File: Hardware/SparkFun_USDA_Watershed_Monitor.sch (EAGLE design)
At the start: 125 parts, among them J10 QWIIC_RIGHT_ANGLE, J12 3-PIN SMD, J3 QWIIC_RIGHT_ANGLE, J4 U.FL, J5 RJ45, J7 RJ45, J9 RJ45, Q1 20V/4.2A/52mΩ/1.4W, Q10 20V/4.2A/52mΩ/1.4W, Q11 20V/0.2A/8MHz/1.2Ω/1Vth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

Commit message: Update GPIO net names
Include both the ESP GPIO number, and the destination
Required schematic to be nudged around in a couple places
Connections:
- net !RFM_CS! renamed ESP_IO15/!RFM_CS!
- net !RFM_RST! renamed ESP_IO5/!RFM_RST!
- net ESP_I36 renamed ESP_I36/GPS_TX
- net ESP_INT_COM renamed ESP_IO4/INT_COM
- net ESP_IO0_BOOT renamed ESP_IO0/BOOT
- net ESP_IO16 renamed ESP_IO16/VOUT
- net ESP_RX renamed ESP_IO3/ESP_RX
- net ESP_TX renamed ESP_IO1/ESP_TX
- net PICO renamed ESP_IO13/PICO
- net POCI renamed ESP_IO12/POCI
- net RFM_IO0 renamed ESP_IO27/RFM_IO0
- net RFM_IO1 renamed ESP_IO26/RFM_IO1
- net SCK renamed ESP_IO14/SCK
- net SCL renamed ESP_IO22/SCL
- net SDA renamed ESP_IO21/SDA
- net STAT renamed ESP_IO2/STAT
- net V_BATT_2 renamed ESP_IO32/V_BATT_2
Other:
- moved on the sheet: BOOT, C14, C19, C20, C21, C22, C23, C4, C5, C6, CHG, D2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

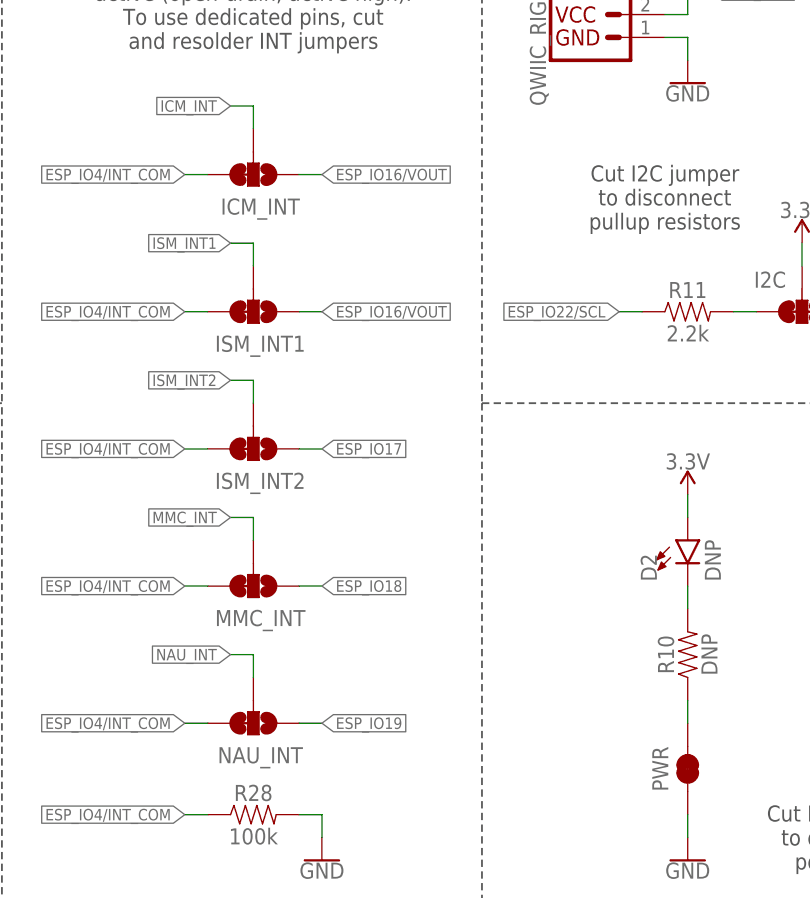
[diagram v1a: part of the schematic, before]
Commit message: Reorder alternative interrupt pins
ESP16 was shared between an alternative interrupt, and the power control
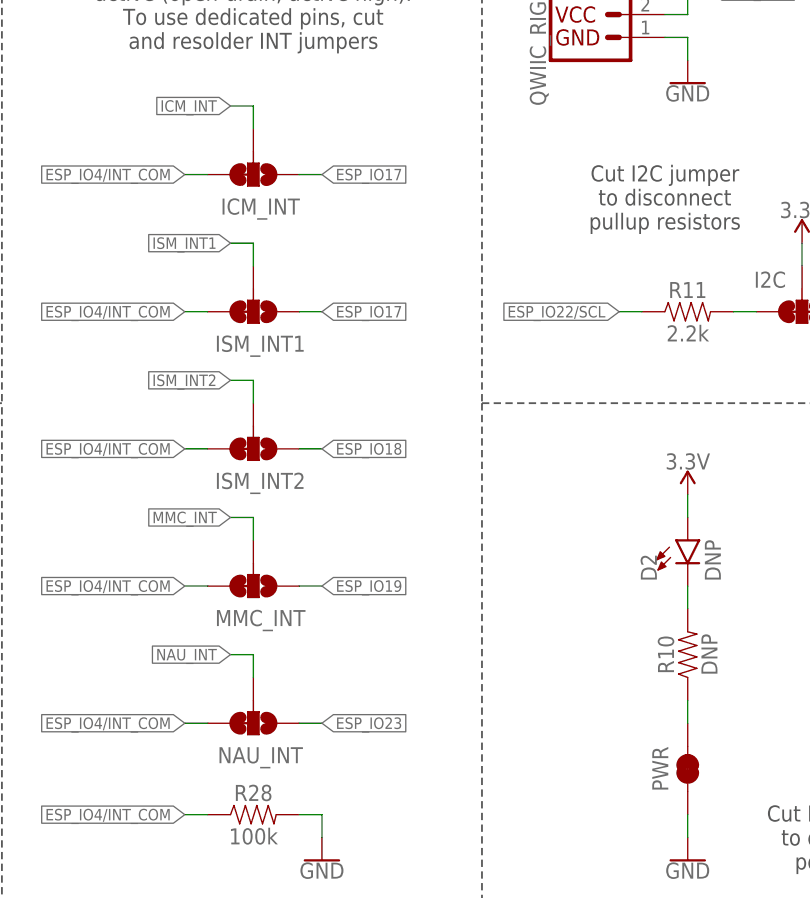
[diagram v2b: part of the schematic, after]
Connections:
- net ESP_IO16/VOUT: no longer ICM_INT.1, ISM_INT1.1
- net ESP_IO17: now also ICM_INT.1, ISM_INT1.1; no longer ISM_INT2.1
- net ESP_IO18: now also ISM_INT2.1; no longer MMC_INT.1
- net ESP_IO19: now also MMC_INT.1; no longer NAU_INT.1
- net ESP_IO23: now also NAU_INT.1
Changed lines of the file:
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@@
-</segment>
-<segment>
-<pinref part="ISM_INT1" gate="G$1" pin="1"/>
-<wire x1="337.82" y1="160.02" x2="340.36" y2="160.02" width="0.1524" layer="91"/>
-<label x="340.36" y="160.02" size="1.27" layer="95" font="vector" xref="yes"/>
-</segment>
-<segment>
-<pinref part="ICM_INT" gate="G$1" pin="1"/>
-<wire x1="337.82" y1="175.26" x2="340.36" y2="175.26" width="0.1524" layer="91"/>
-<label x="340.36" y="175.26" size="1.27" layer="95" font="vector" xref="yes"/>
 </segment>
 <segment>
@@
 </segment>
 <segment>
-<pinref part="ISM_INT2" gate="G$1" pin="1"/>
-<wire x1="337.82" y1="144.78" x2="340.36" y2="144.78" width="0.1524" layer="91"/>
-<label x="340.36" y="144.78" size="1.27" layer="95" font="vector" xref="yes"/>
-</segment>
-<segment>
 <wire x1="307.34" y1="30.48" x2="294.64" y2="30.48" width="0.1524" layer="91"/>
 <label x="294.64" y="30.48" size="1.27" layer="95" font="vector" rot="R180" xref="yes"/>
 <pinref part="J9" gate="JP1" pin="1"/>
+</segment>
+<segment>
+<wire x1="337.82" y1="160.02" x2="340.36" y2="160.02" width="0.1524" layer="91"/>
+<label x="340.36" y="160.02" size="1.27" layer="95" font="vector" xref="yes"/>
+<pinref part="ISM_INT1" gate="G$1" pin="1"/>
+</segment>
+<segment>
+<wire x1="337.82" y1="175.26" x2="340.36" y2="175.26" width="0.1524" layer="91"/>
+<label x="340.36" y="175.26" size="1.27" layer="95" font="vector" xref="yes"/>
+<pinref part="ICM_INT" gate="G$1" pin="1"/>
 </segment>
 </net>
@@
 </segment>
 <segment>
-<pinref part="MMC_INT" gate="G$1" pin="1"/>
-<wire x1="337.82" y1="129.54" x2="340.36" y2="129.54" width="0.1524" layer="91"/>
-<label x="340.36" y="129.54" size="1.27" layer="95" font="vector" xref="yes"/>
-</segment>
-<segment>
 <wire x1="307.34" y1="27.94" x2="294.64" y2="27.94" width="0.1524" layer="91"/>
 <label x="294.64" y="27.94" size="1.27" layer="95" font="vector" rot="R180" xref="yes"/>
 <pinref part="J9" gate="JP1" pin="2"/>
+</segment>
+<segment>
+<wire x1="337.82" y1="144.78" x2="340.36" y2="144.78" width="0.1524" layer="91"/>
+<label x="340.36" y="144.78" size="1.27" layer="95" font="vector" xref="yes"/>
+<pinref part="ISM_INT2" gate="G$1" pin="1"/>
 </segment>
 </net>
@@
 </segment>
 <segment>
-<pinref part="NAU_INT" gate="G$1" pin="1"/>
-<wire x1="337.82" y1="114.3" x2="340.36" y2="114.3" width="0.1524" layer="91"/>
-<label x="340.36" y="114.3" size="1.27" layer="95" font="vector" xref="yes"/>
-</segment>
-<segment>
 <wire x1="307.34" y1="25.4" x2="294.64" y2="25.4" width="0.1524" layer="91"/>
 <label x="294.64" y="25.4" size="1.27" layer="95" font="vector" rot="R180" xref="yes"/>
 <pinref part="J9" gate="JP1" pin="3"/>
+</segment>
+<segment>
+<wire x1="337.82" y1="129.54" x2="340.36" y2="129.54" width="0.1524" layer="91"/>
+<label x="340.36" y="129.54" size="1.27" layer="95" font="vector" xref="yes"/>
+<pinref part="MMC_INT" gate="G$1" pin="1"/>
 </segment>
 </net>
@@
 <pinref part="J9" gate="JP1" pin="4"/>
 </segment>
+<segment>
+<pinref part="NAU_INT" gate="G$1" pin="1"/>
+<wire x1="337.82" y1="114.3" x2="340.36" y2="114.3" width="0.1524" layer="91"/>
+<label x="340.36" y="114.3" size="1.27" layer="95" font="vector" xref="yes"/>
+</segment>
 </net>

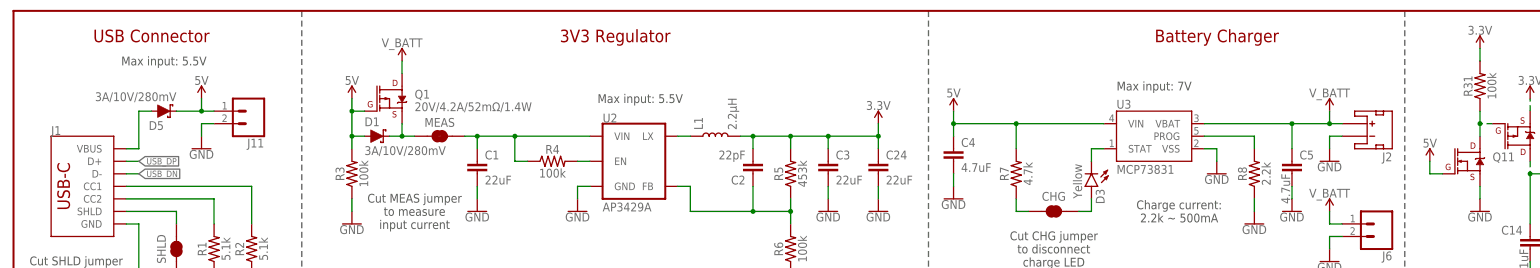
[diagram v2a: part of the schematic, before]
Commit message: Change CH340 power control to be based on VUSB instead of 5V net
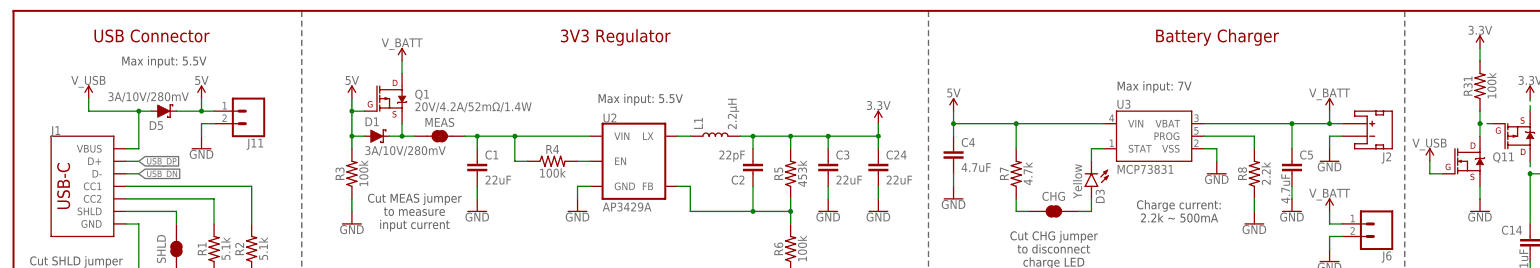
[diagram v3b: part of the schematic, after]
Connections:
- net 5V: no longer Q11.G
- net V_USB: now also Q11.G
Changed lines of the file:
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@@
 <part name="R31" library="SparkFun-Resistors" deviceset="100KOHM" device="-0603-1/10W-1%" value="100k"/>
 <part name="GND63" library="SparkFun-PowerSymbols" deviceset="GND" device=""/>
-<part name="SUPPLY56" library="SparkFun-PowerSymbols" deviceset="5V" device=""/>
 <part name="SUPPLY31" library="SparkFun-PowerSymbols" deviceset="3.3V" device=""/>
 <part name="SUPPLY57" library="SparkFun-PowerSymbols" deviceset="3.3V" device=""/>
 <part name="SUPPLY58" library="SparkFun-PowerSymbols" deviceset="VOUT" device=""/>
+<part name="SUPPLY59" library="SparkFun-PowerSymbols" deviceset="V_USB" device=""/>
+<part name="SUPPLY60" library="SparkFun-PowerSymbols" deviceset="V_USB" device=""/>
 </parts>
 <sheets>
@@
 <instance part="D5" gate="G$1" x="30.48" y="259.08" smashed="yes">
 <attribute name="NAME" x="30.48" y="257.048" size="1.778" layer="95" font="vector" rot="R180"/>
-<attribute name="VALUE" x="33.02" y="261.112" size="1.778" layer="96" font="vector" rot="R180" align="top-left"/>
+<attribute name="VALUE" x="35.56" y="261.112" size="1.778" layer="96" font="vector" rot="R180" align="top-left"/>
 </instance>
 <instance part="SUPPLY2" gate="G$1" x="38.1" y="261.62" smashed="yes">
@@
 <attribute name="VALUE" x="297.18" y="238.506" size="1.778" layer="96" font="vector" align="top-center"/>
 </instance>
-<instance part="SUPPLY56" gate="G$1" x="287.02" y="248.92" smashed="yes">
-<attribute name="VALUE" x="287.02" y="251.714" size="1.778" layer="96" font="vector" align="bottom-center"/>
-</instance>
 <instance part="SUPPLY31" gate="G$1" x="307.34" y="261.62" smashed="yes">
 <attribute name="VALUE" x="307.34" y="264.414" size="1.778" layer="96" font="vector" align="bottom-center"/>
@@
 <instance part="SUPPLY58" gate="G$1" x="297.18" y="33.02" smashed="yes">
 <attribute name="VALUE" x="297.18" y="35.814" size="1.778" layer="96" font="vector" align="bottom-center"/>
+</instance>
+<instance part="SUPPLY59" gate="G$1" x="15.24" y="261.62" smashed="yes">
+<attribute name="VALUE" x="15.24" y="264.414" size="1.778" layer="96" font="vector" align="bottom-center"/>
+</instance>
+<instance part="SUPPLY60" gate="G$1" x="287.02" y="248.92" smashed="yes">
+<attribute name="VALUE" x="287.02" y="251.714" size="1.778" layer="96" font="vector" align="bottom-center"/>
 </instance>
 </instances>
@@
 <wire x1="25.4" y1="259.08" x2="25.4" y2="251.46" width="0.1524" layer="91"/>
 <wire x1="25.4" y1="251.46" x2="22.86" y2="251.46" width="0.1524" layer="91"/>
+<pinref part="SUPPLY59" gate="G$1" pin="V_USB"/>
+<junction x="25.4" y="259.08"/>
+<wire x1="15.24" y1="261.62" x2="15.24" y2="259.08" width="0.1524" layer="91"/>
+<wire x1="15.24" y1="259.08" x2="25.4" y2="259.08" width="0.1524" layer="91"/>
+</segment>
+<segment>
+<pinref part="Q11" gate="NMOS" pin="G"/>
+<wire x1="289.56" y1="246.38" x2="287.02" y2="246.38" width="0.1524" layer="91"/>
+<wire x1="287.02" y1="246.38" x2="287.02" y2="248.92" width="0.1524" layer="91"/>
+<pinref part="SUPPLY60" gate="G$1" pin="V_USB"/>
 </segment>
 </net>
@@
 <pinref part="SUPPLY3" gate="G$1" pin="5V"/>
 </segment>
-<segment>
-<pinref part="Q11" gate="NMOS" pin="G"/>
-<pinref part="SUPPLY56" gate="G$1" pin="5V"/>
-<wire x1="289.56" y1="246.38" x2="287.02" y2="246.38" width="0.1524" layer="91"/>
-<wire x1="287.02" y1="246.38" x2="287.02" y2="248.92" width="0.1524" layer="91"/>
-</segment>
-</net>
+</net>

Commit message: Fix load cell B+/- pinout
Update to match silkscreen
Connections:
- net NAU_B+: now also J5.4; no longer J5.5
- net NAU_B-: now also J5.5; no longer J5.4
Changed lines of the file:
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@@
 </segment>
 <segment>
-<pinref part="J5" gate="JP1" pin="4"/>
-<wire x1="261.62" y1="22.86" x2="254" y2="22.86" width="0.1524" layer="91"/>
-<label x="254" y="22.86" size="1.27" layer="95" font="vector" rot="R180" xref="yes"/>
+<wire x1="261.62" y1="20.32" x2="254" y2="20.32" width="0.1524" layer="91"/>
+<label x="254" y="20.32" size="1.27" layer="95" font="vector" rot="R180" xref="yes"/>
+<pinref part="J5" gate="JP1" pin="5"/>
 </segment>
 </net>
@@
 </segment>
 <segment>
-<pinref part="J5" gate="JP1" pin="5"/>
-<wire x1="261.62" y1="20.32" x2="254" y2="20.32" width="0.1524" layer="91"/>
-<label x="254" y="20.32" size="1.27" layer="95" font="vector" rot="R180" xref="yes"/>
+<wire x1="261.62" y1="22.86" x2="254" y2="22.86" width="0.1524" layer="91"/>
+<label x="254" y="22.86" size="1.27" layer="95" font="vector" rot="R180" xref="yes"/>
+<pinref part="J5" gate="JP1" pin="4"/>
 </segment>
 </net>

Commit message: Add note to schematic about CH340 power
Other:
- note added: "CH340 will be powered down when V_USB is not present for low-power applications. Note that ESP_IO1/3 should be disabled in this case to prevent back powering the CH340"
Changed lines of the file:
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@@
 <wire x1="281.94" y1="215.9" x2="281.94" y2="279.4" width="0.1524" layer="97" style="longdash"/>
 <wire x1="368.3" y1="215.9" x2="368.3" y2="279.4" width="0.2032" layer="97" style="longdash"/>
+<text x="337.82" y="261.62" size="1.778" layer="97" font="vector" align="center">CH340 will be powered down when
+V_USB is not present for low-power
+applications. Note that ESP_IO1/3
+should be disabled in this case to
+prevent back powering the CH340</text>
 </plain>
 <instances>

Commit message: Add note about VOUT to schematic
Add note instructing how to enable VOUT
Rename net to !VOUT_EN!
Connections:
- net ESP_IO16/VOUT renamed ESP_IO16/!VOUT_EN!
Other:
- note added: "Drive ESP_IO16 low to enable VOUT, which powers onboard sensors and LoRa module, plus connected peripherals"
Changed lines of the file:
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@@
 should be disabled in this case to
 prevent back powering the CH340</text>
+<text x="274.32" y="104.14" size="1.778" layer="97" font="vector" align="center">Drive ESP_IO16 low to
+enable VOUT, which
+powers onboard sensors
+and LoRa module, plus
+connected peripherals</text>
 </plain>
 <instances>
@@
 </segment>
 </net>
-<net name="ESP_IO16/VOUT" class="0">
+<net name="ESP_IO16/!VOUT_EN!" class="0">
 <segment>
 <pinref part="U1" gate="U1" pin="IO16"/>

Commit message: Change DIO-14072 for DIO-11623
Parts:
- D1, D5, D6: value 3A/10V/280mV -> 1A/23V/620mV; device SparkFun-DiscreteSemi:DIODE-SCHOTTKY-BAT60A -> SparkFun-DiscreteSemi:DIODE-SCHOTTKY-BAT20J
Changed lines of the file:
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@@
 <part name="MEAS" library="SparkFun-Jumpers" deviceset="JUMPER-COMBO_2_NC_TRACE" device=""/>
 <part name="Q1" library="SparkFun-DiscreteSemi" deviceset="MOSFET_PCH" device="-DMG2305UX-7" value="20V/4.2A/52mΩ/1.4W"/>
-<part name="D1" library="SparkFun-DiscreteSemi" deviceset="DIODE-SCHOTTKY" device="-BAT60A" value="3A/10V/280mV"/>
+<part name="D1" library="SparkFun-DiscreteSemi" deviceset="DIODE-SCHOTTKY" device="-BAT20J" value="1A/23V/620mV"/>
 <part name="R3" library="SparkFun-Resistors" deviceset="100KOHM" device="-0603-1/10W-1%" value="100k"/>
 <part name="R4" library="SparkFun-Resistors" deviceset="100KOHM" device="-0603-1/10W-1%" value="100k"/>
@@
 <part name="J11" library="SparkFun-Connectors" deviceset="CONN_02" device="1X02_NO_SILK"/>
 <part name="GND57" library="SparkFun-PowerSymbols" deviceset="GND" device=""/>
-<part name="D5" library="SparkFun-DiscreteSemi" deviceset="DIODE-SCHOTTKY" device="-BAT60A" value="3A/10V/280mV"/>
+<part name="D5" library="SparkFun-DiscreteSemi" deviceset="DIODE-SCHOTTKY" device="-BAT20J" value="1A/23V/620mV"/>
 <part name="SUPPLY2" library="SparkFun-PowerSymbols" deviceset="5V" device=""/>
 <part name="SUPPLY49" library="SparkFun-PowerSymbols" deviceset="5V" device=""/>
@@
 <part name="R26" library="SparkFun-Resistors" deviceset="100KOHM" device="-0603-1/10W-1%" value="100k"/>
 <part name="SUPPLY47" library="SparkFun-PowerSymbols" deviceset="3.3V" device=""/>
-<part name="D6" library="SparkFun-DiscreteSemi" deviceset="DIODE-SCHOTTKY" device="-BAT60A" value="3A/10V/280mV"/>
+<part name="D6" library="SparkFun-DiscreteSemi" deviceset="DIODE-SCHOTTKY" device="-BAT20J" value="1A/23V/620mV"/>
 <part name="Q5" library="SparkFun-DiscreteSemi" deviceset="MOSFET_PCH" device="-DMG2305UX-7" value="20V/4.2A/52mΩ/1.4W"/>
 <part name="GND20" library="SparkFun-PowerSymbols" deviceset="GND" device=""/>

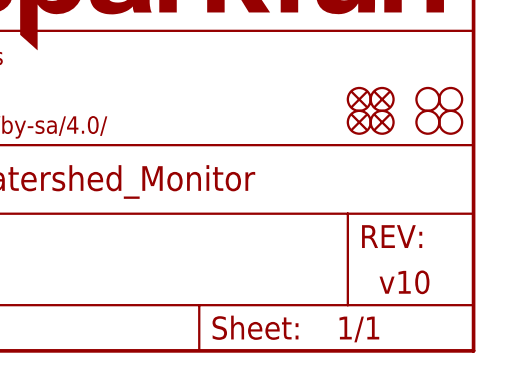
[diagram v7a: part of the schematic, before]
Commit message: v11 updates
Bump version number to v11
Remove USDA from silkscreen
Repanelize
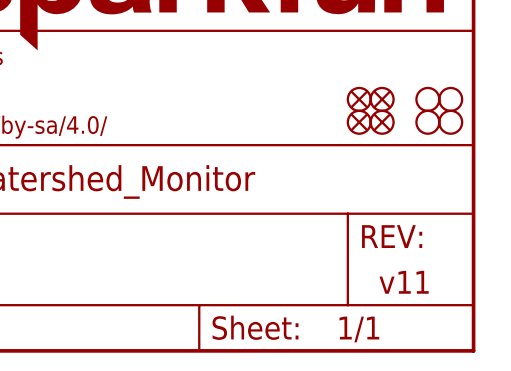
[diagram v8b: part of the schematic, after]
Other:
- note added: "v11"
- note removed: "v10"
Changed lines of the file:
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@@
 <plain>
 <text x="358.14" y="12.7" size="2.54" layer="94" font="vector" align="center">Dryw Wade</text>
-<text x="424.18" y="7.62" size="2.54" layer="94" font="vector" align="center">v10</text>
+<text x="424.18" y="7.62" size="2.54" layer="94" font="vector" align="center">v11</text>
 <text x="27.94" y="274.32" size="2.54" layer="94" font="vector" align="center">USB Connector</text>
 <text x="121.92" y="274.32" size="2.54" layer="94" font="vector" align="center">3V3 Regulator</text>
